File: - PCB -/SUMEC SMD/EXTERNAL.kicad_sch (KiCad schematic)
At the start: 10 parts, among them Q1 S8050, Q2 S8050, U1 CP2102N-Axx-xQFN28

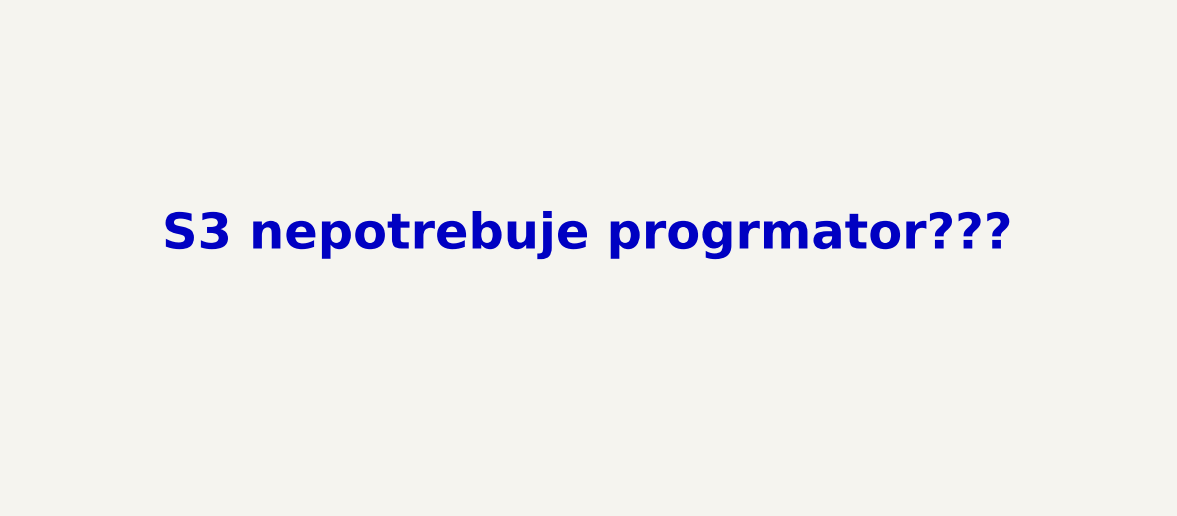
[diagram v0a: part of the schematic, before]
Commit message: pcb update boot and enable pins
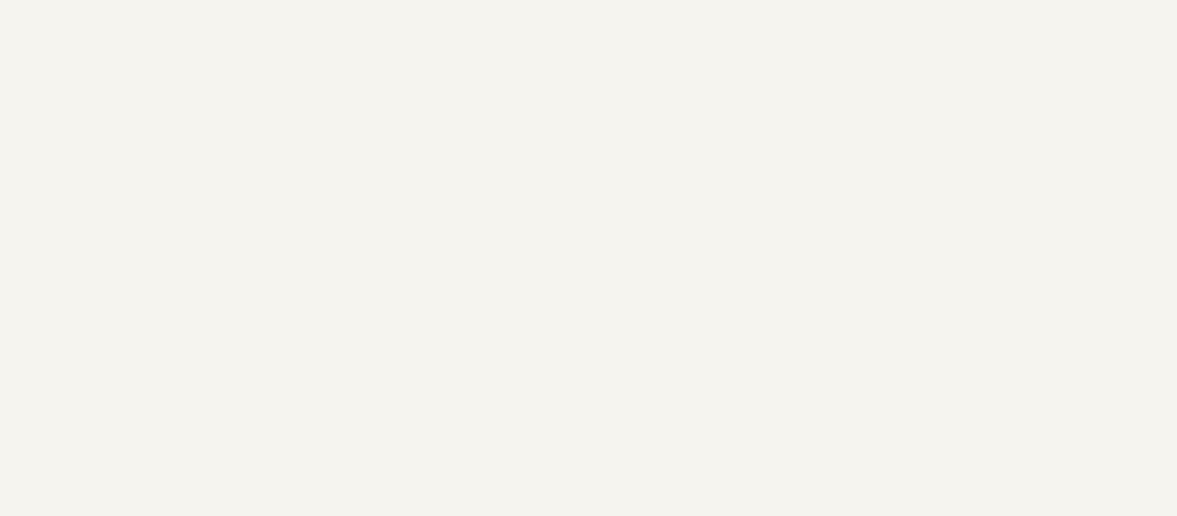
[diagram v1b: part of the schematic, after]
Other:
- note removed: "S3 nepotrebuje progrmator???"
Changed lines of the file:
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@@
     (effects (font (size 2 2) (thickness 0.4) bold) (justify left bottom))
-  )
-  (text "S3 nepotrebuje progrmator???" (at 237.49 43.18 0)
-    (effects (font (size 4 4) bold (color 255 0 0 1)) (justify left bottom))
   )
   (text "DOWNLOADER" (at 105.41 127 0)

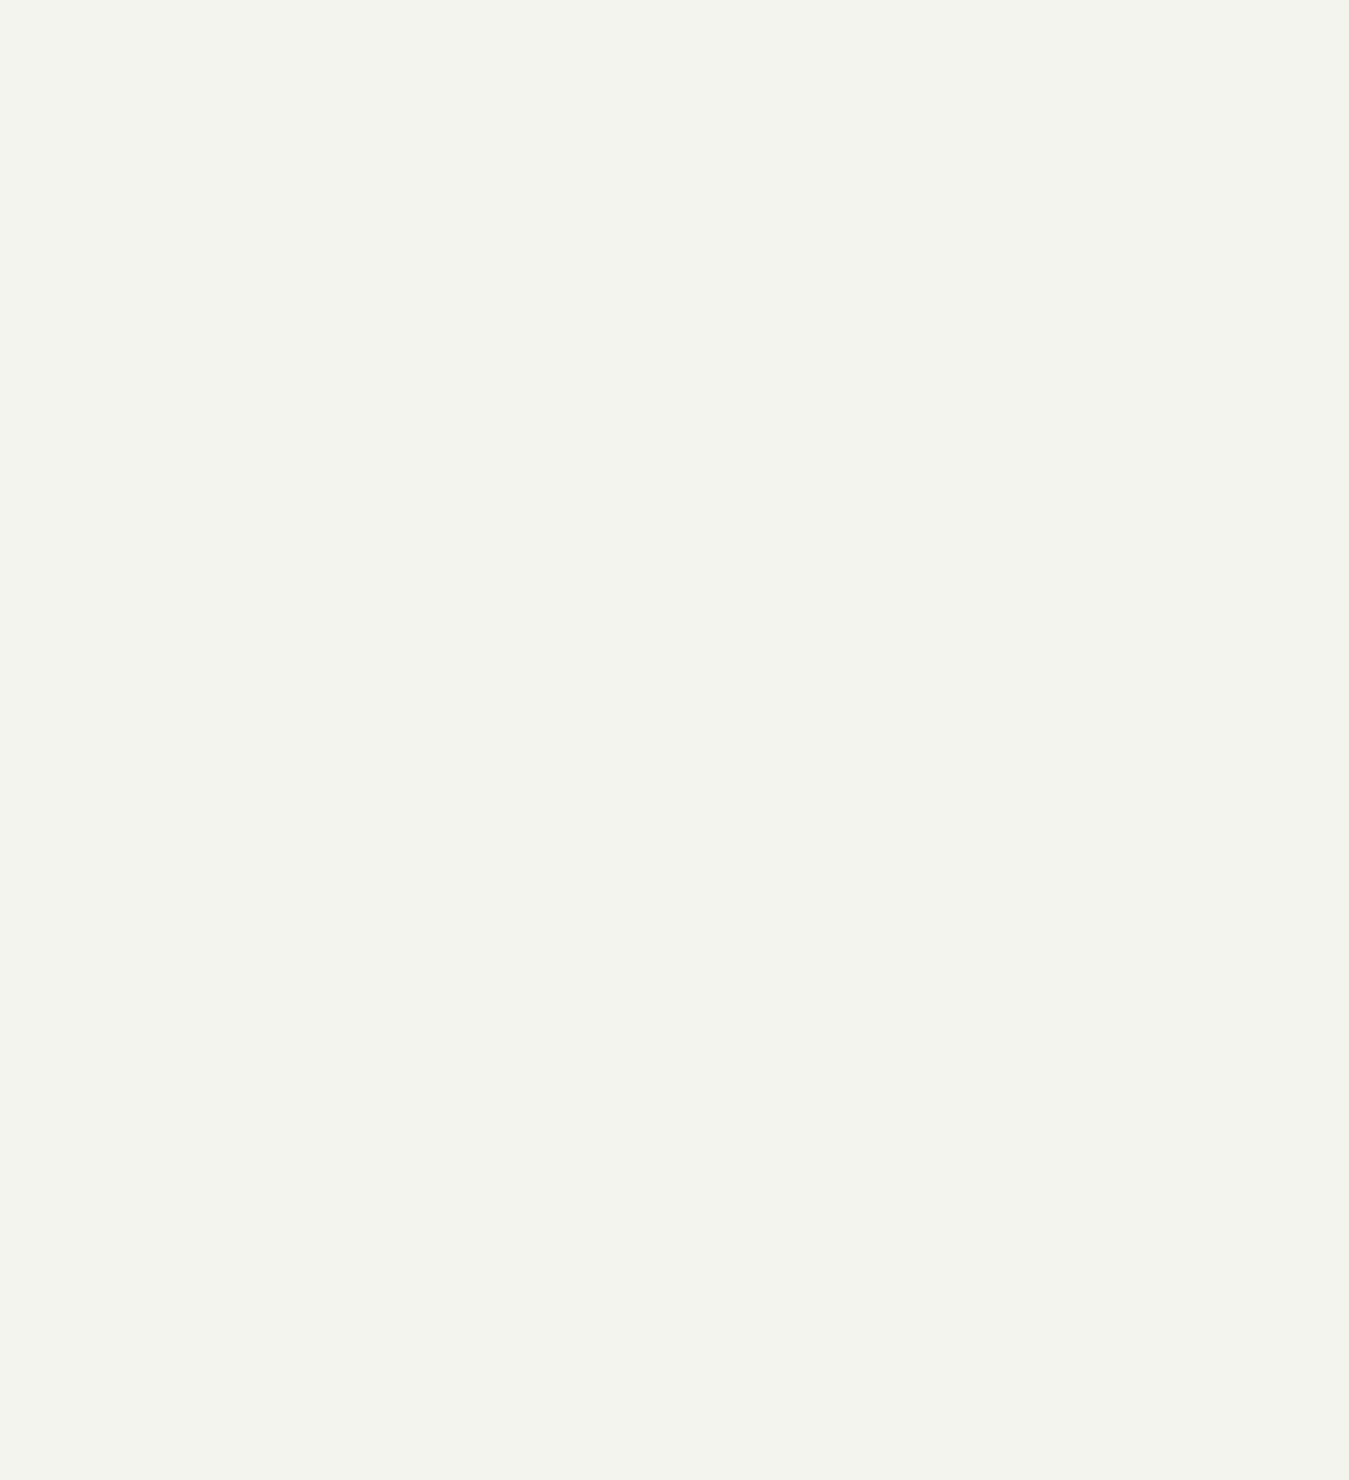
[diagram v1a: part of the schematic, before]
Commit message: PCB Update - "LIDAR"sensors
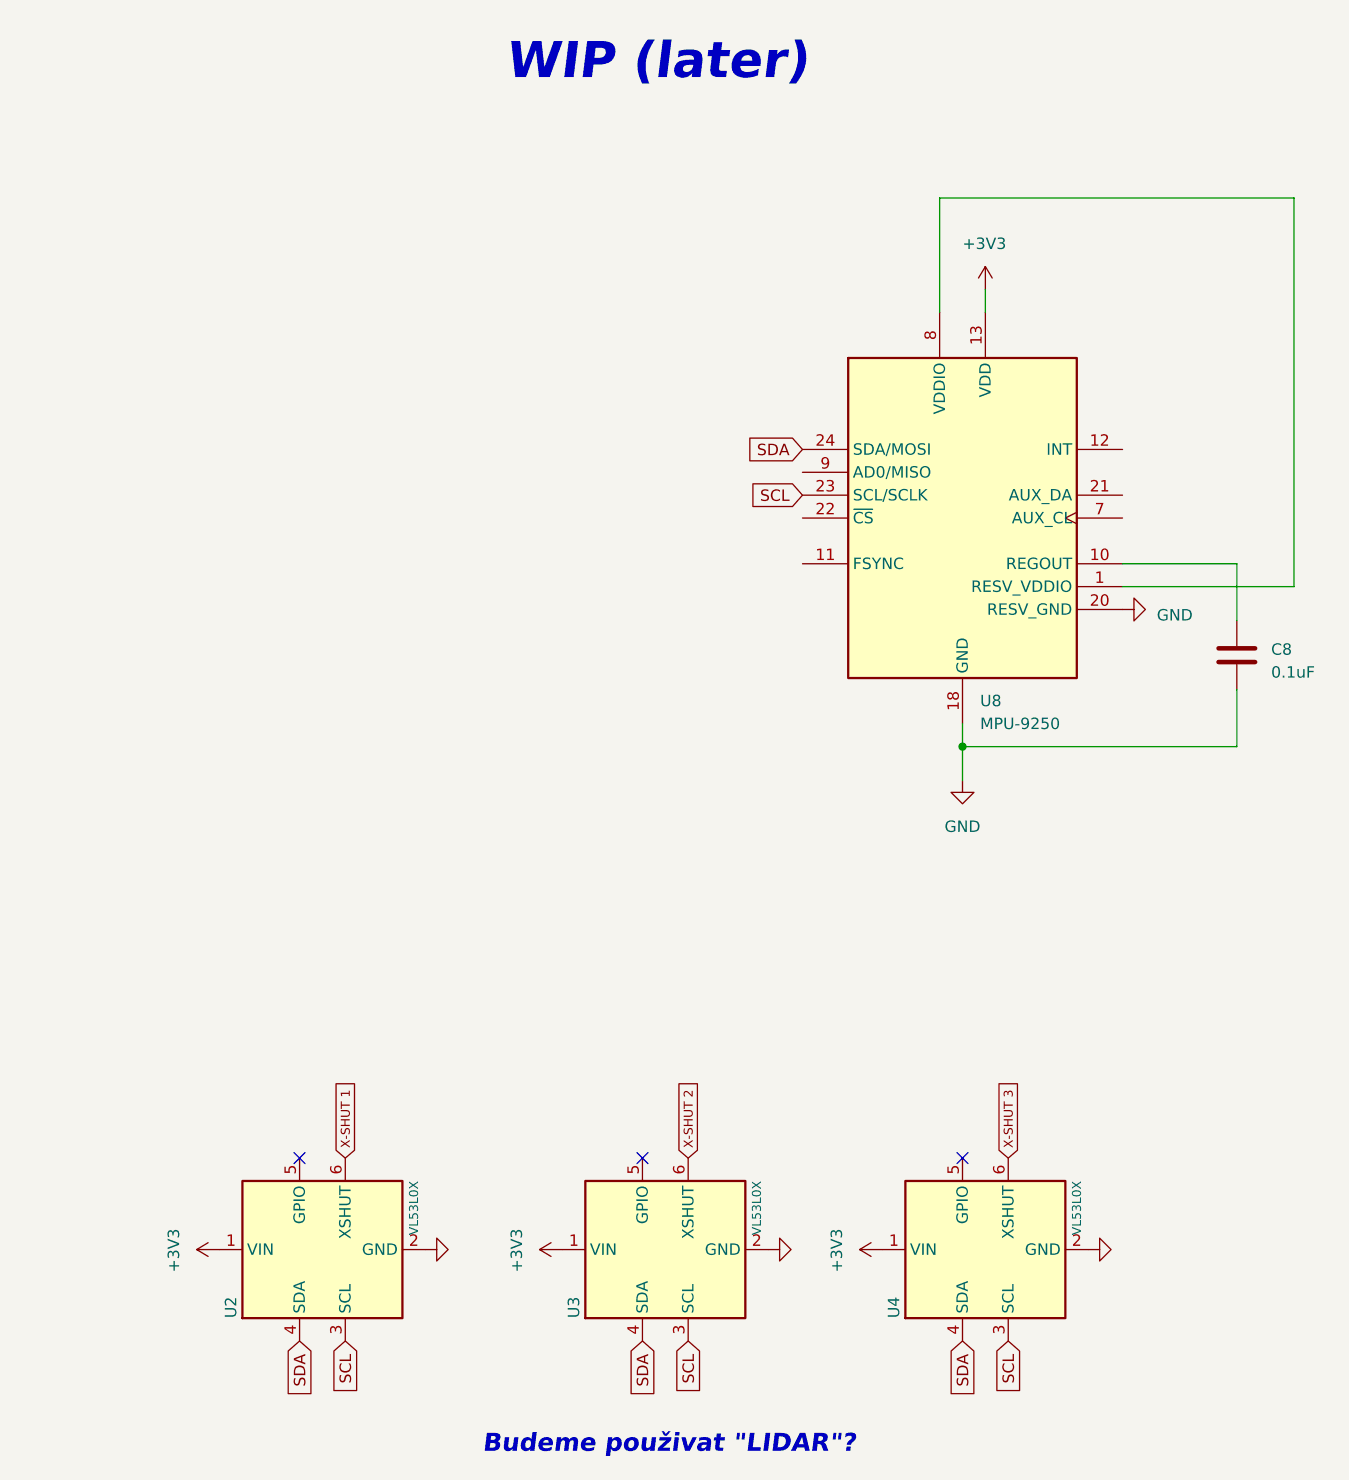
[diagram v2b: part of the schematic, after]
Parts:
- added C8: 0.1uF, Capacitor_SMD:C_1206_3216Metric, symbol Device:C
- added U2, U3, U4: VL53L0X, sumec-smd_library:GY-530 VL53L0X, symbol sumec_library:GY-530_VL53L0X
- added U8: MPU-9250, symbol Sensor_Motion:MPU-9250
- Q1, Q2: footprint Package_TO_SOT_THT:TO-92L -> (none)
- R14, R15: footprint Resistor_SMD:R_1206_3216Metric -> (none)
- U1: footprint Package_DFN_QFN:QFN-28-1EP_5x5mm_P0.5mm_EP3.35x3.35mm -> (none)
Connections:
- net +3V3: now also U2.1 (VIN), U3.1 (VIN), U4.1 (VIN), U8.13 (VDD)
- net GND: now also C8.2, U2.2 (GND), U3.2 (GND), U4.2 (GND), U8.18 (GND), U8.20 (RESV_GND)
- new net: C8.1, U8.10 (REGOUT)
- new net: U8.1 (RESV_VDDIO), U8.8 (VDDIO)
- new net SCL: U2.3 (SCL), U3.3 (SCL), U4.3 (SCL), U8.23 (SCL/SCLK)
- new net SDA: U2.4 (SDA), U3.4 (SDA), U4.4 (SDA), U8.24 (SDA/MOSI)
- new net X-SHUT 1: U2.6 (XSHUT)
- new net X-SHUT 2: U3.6 (XSHUT)
- new net X-SHUT 3: U4.6 (XSHUT)
- no-connect marks 15 -> 18
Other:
- note added: "Budeme použivat "LIDAR"?"
- note added: "WIP (later)"
